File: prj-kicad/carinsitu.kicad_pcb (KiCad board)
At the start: 4 copper layers, 131.5 x 50 mm, 31 parts, among them P1 BAT, P2 MOT, SW1 SWITCH_SLIDE, U1 ESP32, U2 MIC2860, U3 STC3100, X1 40MHz

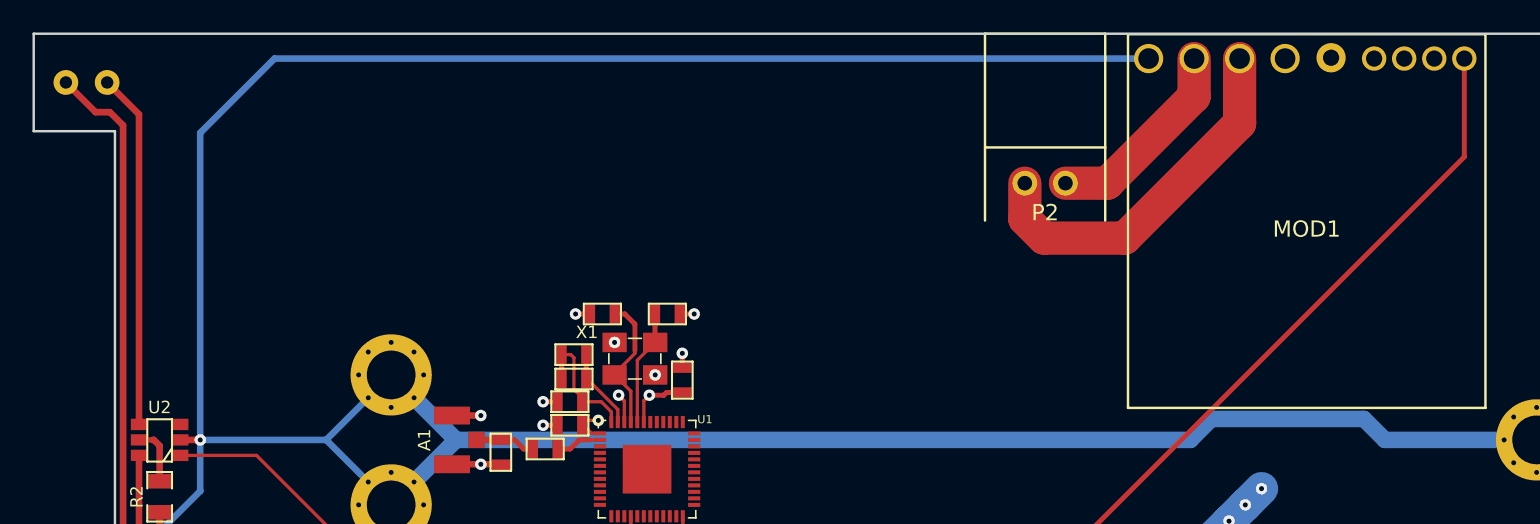
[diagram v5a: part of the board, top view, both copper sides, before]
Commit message: = ADD: insert a 3 pin connector for servo (direction)
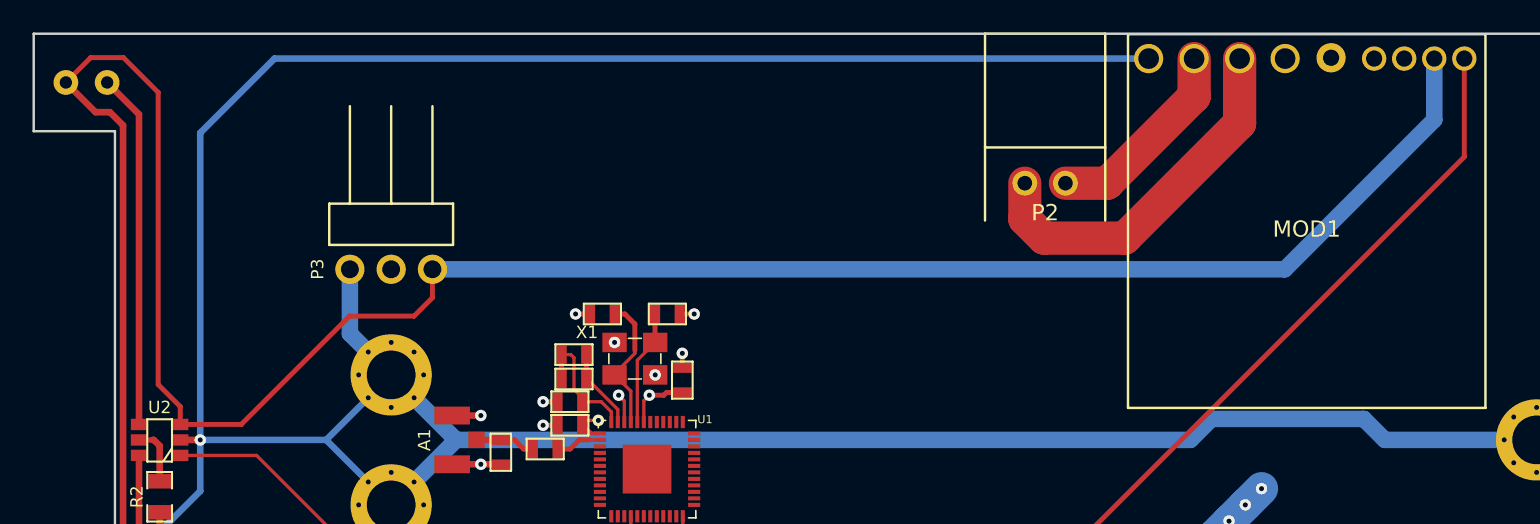
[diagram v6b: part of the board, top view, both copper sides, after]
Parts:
- added P3: CONN_3, carinsitu:CONN_61300311021, F.Cu at (104.8, 94.5)
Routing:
- net +5V: track 48.2 -> 166.1 mm
- net GND: track 309.8 -> 344.2 mm
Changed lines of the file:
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@@
 (kicad_pcb (version 4) (host pcbnew 4.0.2+dfsg1-stable)
   (general
-    (links 99)
-    (no_connects 5)
-    (area 82.674999 79.924999 214.315001 130.075001)
+    (links 101)
+    (no_connects 2)
+    (area 73.750001 78.949999 214.315001 133.950001)
     (thickness 1.6)
     (drawings 27)
-    (tracks 223)
+    (tracks 241)
     (zones 0)
-    (modules 31)
-    (nets 64)
+    (modules 32)
+    (nets 65)
   )
   (page A4)
@@
   )
   (setup
-    (last_trace_width 1.016)
+    (last_trace_width 0.3048)
     (user_trace_width 0.2032)
     (user_trace_width 0.3048)
@@
   (net 62 SDA)
   (net 63 SCL)
+  (net 64 SERVO_PWM)
   (net_class Default "This is the default net class."
     (clearance 0.1524)
@@
     (add_net SCL)
     (add_net SDA)
+    (add_net SERVO_PWM)
   )
   (module carinsitu:FIX locked (layer F.Cu)
@@
     )
   )
+  (module carinsitu:CONN_61300311021 (layer F.Cu)
+    (at 104.75 94.5 180)
+    (fp_text reference P3 (at 4.53 0.01 270) (layer F.SilkS)
+      (effects (font (size 0.762 0.762) (thickness 0.1016)))
+    )
+    (fp_text value CONN_3 (at 0 -1.4 180) (layer F.Fab)
+      (effects (font (size 0.762 0.762) (thickness 0.1016)))
+    )
+    (fp_line (start 2.54 4.04) (end 2.54 10.04) (layer F.SilkS) (width 0.15))
+    (fp_line (start 0 4.04) (end 0 10.04) (layer F.SilkS) (width 0.15))
+    (fp_line (start -2.54 4.04) (end -2.54 10.04) (layer F.SilkS) (width 0.15))
+    (fp_line (start -3.81 1.5) (end 3.81 1.5) (layer F.SilkS) (width 0.15))
+    (fp_line (start 3.81 1.5) (end 3.81 4.04) (layer F.SilkS) (width 0.15))
+    (fp_line (start 3.81 4.04) (end -3.81 4.04) (layer F.SilkS) (width 0.15))
+    (fp_line (start -3.81 4.04) (end -3.81 1.5) (layer F.SilkS) (width 0.15))
+    (pad 1 thru_hole circle (at -2.54 0 180) (size 1.8 1.8) (drill 1.1) (layers *.Cu *.Mask)
+      (net 3 +5V))
+    (pad 2 thru_hole circle (at 0 0 180) (size 1.8 1.8) (drill 1.1) (layers *.Cu *.Mask F.SilkS)
+      (net 64 SERVO_PWM))
+    (pad 3 thru_hole circle (at 2.54 0 180) (size 1.8 1.8) (drill 1.1) (layers *.Cu *.Mask F.SilkS)
+      (net 1 GND))
+  )
   (gr_text + (at 92 121.27) (layer F.SilkS)
     (effects (font (size 1.5 1.5) (thickness 0.3)))
@@
   (gr_line (start 213.21 80) (end 214.24 82.48) (angle 90) (layer Edge.Cuts) (width 0.15))
   (gr_line (start 82.75 80) (end 213.21 80) (angle 90) (layer Edge.Cuts) (width 0.15))
+  (segment (start 167.1 81.53) (end 167.1 96.85) (width 1.016) (layer In2.Cu) (net 1) (status 400000))
+  (segment (start 167.1 96.85) (end 175.25 105) (width 1.016) (layer In2.Cu) (net 1) (status 800000))
+  (segment (start 102.21 94.5) (end 102.21 98.46) (width 1.016) (layer B.Cu) (net 1) (status 400000))
+  (segment (start 102.21 98.46) (end 104.75 101) (width 1.016) (layer B.Cu) (net 1) (status 800000))
   (segment (start 90.5 110.65) (end 90.5 112.03) (width 1.016) (layer B.Cu) (net 1))
   (via (at 92 113.53) (size 0.7112) (drill 0.3048) (layers F.Cu B.Cu) (net 1))
@@
   (segment (start 90.5 112.03) (end 92 113.53) (width 1.016) (layer B.Cu) (net 1))
   (segment (start 93.51 114.8) (end 98.95 114.8) (width 1.016) (layer B.Cu) (net 1))
-  (segment (start 98.95 114.8) (end 104.75 109) (width 1.016) (layer B.Cu) (net 1) (status 800000))
+  (segment (start 98.95 114.8) (end 104.75 109) (width 1.016) (layer B.Cu) (net 1))
   (segment (start 92 114.7975) (end 93.5075 114.7975) (width 1.016) (layer F.Cu) (net 1))
   (segment (start 93.5075 114.7975) (end 93.51 114.8) (width 1.016) (layer F.Cu) (net 1))
@@
   (segment (start 96.685 126.955) (end 96.68 126.95) (width 0.3048) (layer F.Cu) (net 1))
   (via (at 96.68 126.95) (size 0.7112) (drill 0.3048) (layers F.Cu B.Cu) (net 1))
-  (segment (start 97.84 126.955) (end 96.685 126.955) (width 0.3048) (layer F.Cu) (net 1) (status 400000))
+  (segment (start 97.84 126.955) (end 96.685 126.955) (width 0.3048) (layer F.Cu) (net 1))
   (segment (start 94.66 126.95) (end 91 123.29) (width 0.3048) (layer B.Cu) (net 1))
-  (segment (start 100.288 123.33) (end 99.06 123.33) (width 0.3048) (layer F.Cu) (net 1) (status 400000))
+  (segment (start 100.288 123.33) (end 99.06 123.33) (width 0.3048) (layer F.Cu) (net 1))
   (segment (start 98.57 123.29) (end 98.61 123.33) (width 0.3048) (layer B.Cu) (net 1))
   (segment (start 98.61 123.33) (end 99.06 123.33) (width 0.3048) (layer B.Cu) (net 1))
@@
   (via (at 91 123.29) (size 0.7112) (drill 0.3048) (layers F.Cu B.Cu) (net 1))
   (segment (start 91 123.29) (end 98.57 123.29) (width 0.3048) (layer B.Cu) (net 1))
-  (segment (start 100.288 123.33) (end 100.29 123.328) (width 0.3048) (layer F.Cu) (net 1) (status C00000))
+  (segment (start 100.288 123.33) (end 100.29 123.328) (width 0.3048) (layer F.Cu) (net 1))
   (segment (start 122.67 99.67) (end 122.67 100.44) (width 0.3048) (layer In2.Cu) (net 1))
   (segment (start 122.67 100.44) (end 122.11 101) (width 0.3048) (layer In2.Cu) (net 1))
@@
   (segment (start 149.9 92.58) (end 144.93 92.58) (width 2.048) (layer F.Cu) (net 2))
   (segment (start 156.97 85.51) (end 149.9 92.58) (width 2.048) (layer F.Cu) (net 2))
+  (segment (start 91.77 104.0475) (end 91.77 102.95) (width 0.3048) (layer F.Cu) (net 3) (status 400000))
+  (segment (start 86.26 81.47) (end 84.73 83) (width 0.3048) (layer F.Cu) (net 3) (status 800000))
+  (segment (start 88.27 81.47) (end 86.26 81.47) (width 0.3048) (layer F.Cu) (net 3))
+  (segment (start 90.41 83.61) (end 88.27 81.47) (width 0.3048) (layer F.Cu) (net 3))
+  (segment (start 90.41 101.59) (end 90.41 83.61) (width 0.3048) (layer F.Cu) (net 3))
+  (segment (start 91.77 102.95) (end 90.41 101.59) (width 0.3048) (layer F.Cu) (net 3))
+  (segment (start 91.77 104.0475) (end 95.5225 104.0475) (width 0.3048) (layer F.Cu) (net 3) (status 400000))
+  (segment (start 107.29 96.25) (end 107.29 94.5) (width 0.3048) (layer F.Cu) (net 3) (status 800000))
+  (segment (start 106.16 97.38) (end 107.29 96.25) (width 0.3048) (layer F.Cu) (net 3))
+  (segment (start 102.19 97.38) (end 106.16 97.38) (width 0.3048) (layer F.Cu) (net 3))
+  (segment (start 95.5225 104.0475) (end 102.19 97.38) (width 0.3048) (layer F.Cu) (net 3))
+  (segment (start 107.29 94.5) (end 159.75 94.5) (width 1.016) (layer B.Cu) (net 3) (status 400000))
+  (segment (start 168.95 85.3) (end 168.95 81.53) (width 1.016) (layer B.Cu) (net 3) (status 800000))
+  (segment (start 159.75 94.5) (end 168.95 85.3) (width 1.016) (layer B.Cu) (net 3))
   (segment (start 86.56 84.83) (end 87.44 84.83) (width 0.4064) (layer F.Cu) (net 3))
+  (segment (start 87.44 84.83) (end 88.25 85.64) (width 0.4064) (layer F.Cu) (net 3))
+  (segment (start 86.56 84.83) (end 84.73 83) (width 0.4064) (layer F.Cu) (net 3))
+  (segment (start 86.56 125.17) (end 87.81 125.17) (width 0.4064) (layer F.Cu) (net 3))
+  (segment (start 84.73 127) (end 86.56 125.17) (width 0.4064) (layer F.Cu) (net 3))
+  (segment (start 88.25 124.73) (end 88.25 85.64) (width 0.4064) (layer F.Cu) (net 3))
   (segment (start 87.81 125.17) (end 88.25 124.73) (width 0.4064) (layer F.Cu) (net 3))
-  (segment (start 88.25 124.73) (end 88.25 85.64) (width 0.4064) (layer F.Cu) (net 3))
-  (segment (start 84.73 127) (end 86.56 125.17) (width 0.4064) (layer F.Cu) (net 3))
-  (segment (start 86.56 125.17) (end 87.81 125.17) (width 0.4064) (layer F.Cu) (net 3))
-  (segment (start 86.56 84.83) (end 84.73 83) (width 0.4064) (layer F.Cu) (net 3))
-  (segment (start 87.44 84.83) (end 88.25 85.64) (width 0.4064) (layer F.Cu) (net 3))
   (segment (start 89.23 105.9525) (end 89.23 125.04) (width 0.4064) (layer F.Cu) (net 4))
   (segment (start 89.23 125.04) (end 87.27 127) (width 0.4064) (layer F.Cu) (net 4))
@@
   (segment (start 105.48 121.27) (end 107 122.79) (width 2.048) (layer F.Cu) (net 55))
   (segment (start 107 124.25) (end 107 122.79) (width 2.048) (layer F.Cu) (net 55))
-  (segment (start 100.29 124.852) (end 100.29 125.938) (width 0.3048) (layer F.Cu) (net 56) (status C00000))
-  (segment (start 97.84 125.005) (end 99.085 125.005) (width 0.2032) (layer F.Cu) (net 56) (status 400000))
-  (segment (start 99.238 124.852) (end 100.29 124.852) (width 0.2032) (layer F.Cu) (net 56) (status 800000))
+  (segment (start 100.29 124.852) (end 100.29 125.938) (width 0.3048) (layer F.Cu) (net 56))
+  (segment (start 97.84 125.005) (end 99.085 125.005) (width 0.2032) (layer F.Cu) (net 56))
+  (segment (start 99.238 124.852) (end 100.29 124.852) (width 0.2032) (layer F.Cu) (net 56))
   (segment (start 99.085 125.005) (end 99.238 124.852) (width 0.2032) (layer F.Cu) (net 56))
   (segment (start 105 125.11) (end 103.52 125.11) (width 0.3048) (layer F.Cu) (net 57))

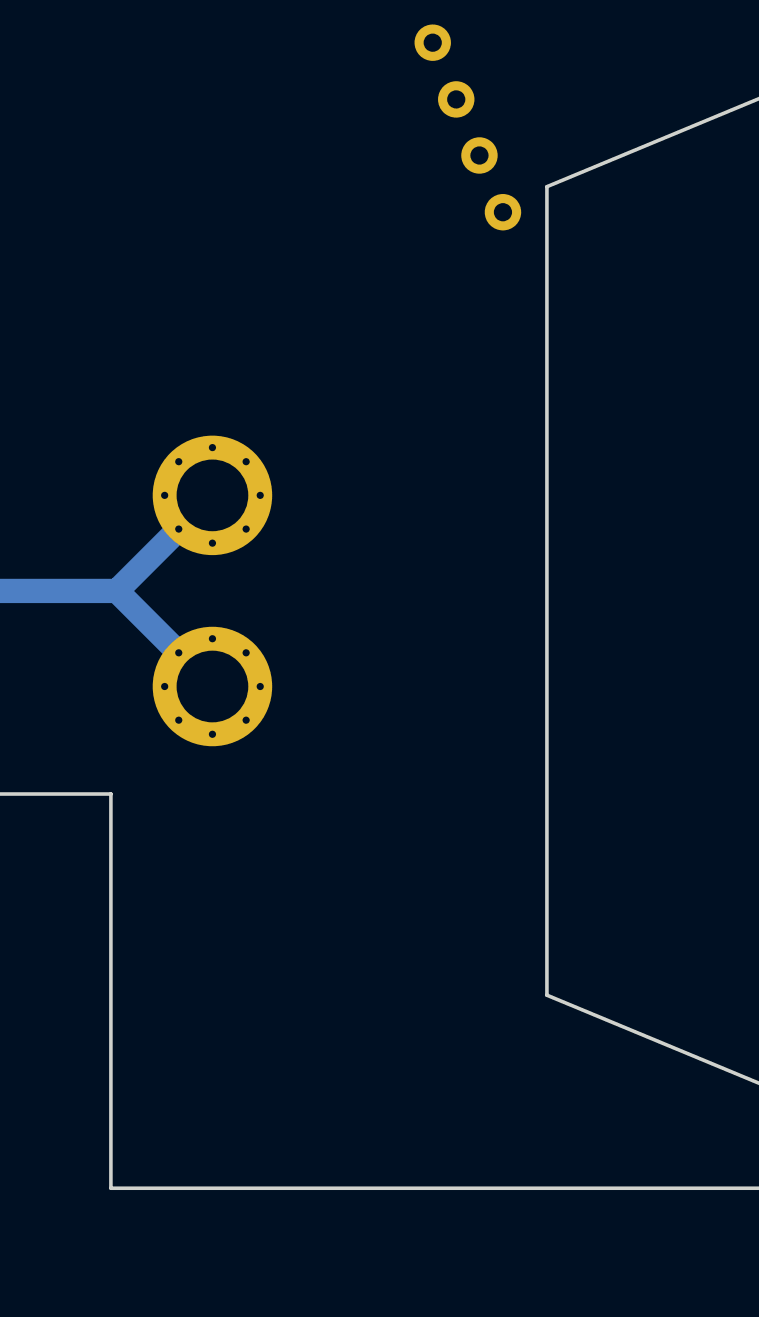
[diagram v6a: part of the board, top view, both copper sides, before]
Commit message: = ADD: insert second RGB led and add a level switch (3V3 -> 5V) on data line
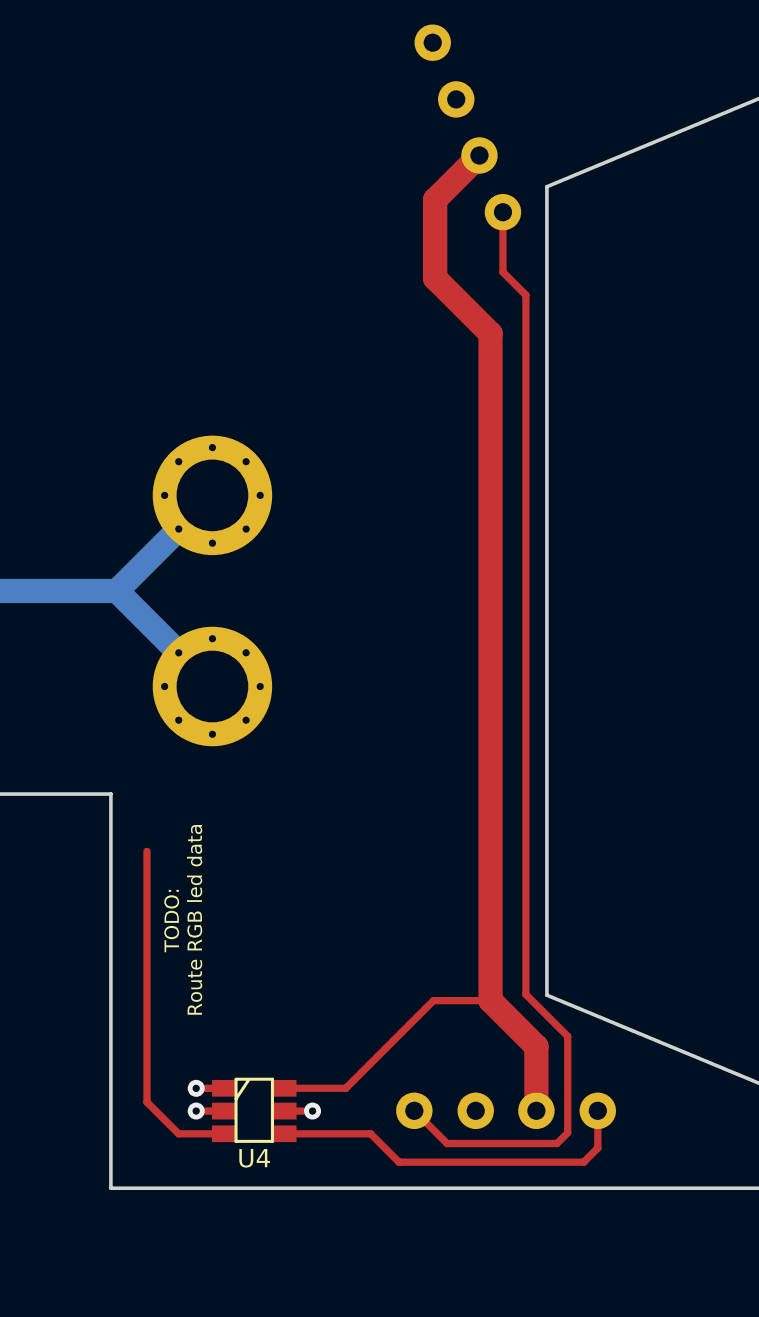
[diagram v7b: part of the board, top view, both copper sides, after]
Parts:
- added D3: LED_APA106, carinsitu:LED-APA106, F.Cu at (199.0, 126.8)
- added U4: SN74LVC1T45, carinsitu:SOT23-6, F.Cu at (188.5, 126.8)
- D4: renamed from REF**; value LED-APA106 -> LED_APA106
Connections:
- D4 pad 1: (no net) -> Net-(D4-Pad1)
- D4 pad 2: (no net) -> GND
- D4 pad 3: (no net) -> +5V
- D4 pad 4: (no net) -> Net-(D3-Pad1)
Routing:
- net GND: track 344.2 -> 404.5 mm, vias 17 -> 18
- net +5V: track 166.1 -> 218.8 mm
- net Net-(D3-Pad1): track 0.00 -> 46.8 mm
- net +3V3: track 12.1 -> 53.7 mm, vias 3 -> 5
- net Net-(D3-Pad4): track 0.00 -> 15.4 mm
- net RL_DAT: track 0.00 -> 14.3 mm
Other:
- board text added: "TODO: Route RGB led data"

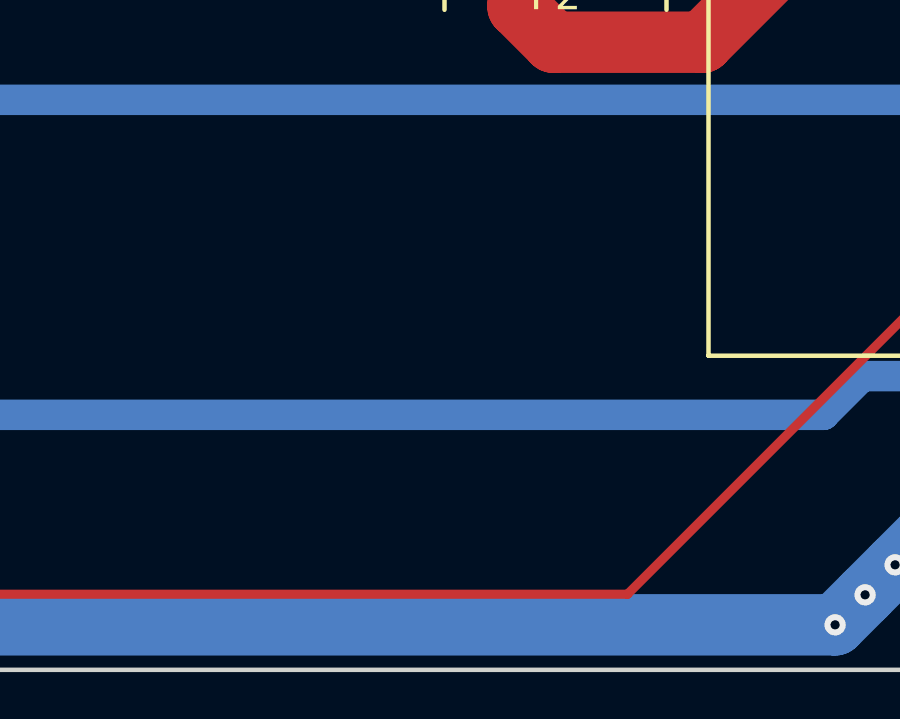
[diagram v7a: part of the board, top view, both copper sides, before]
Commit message: = ADD: insert a 3V3 power regulator. Schematic and place ok, routing not complete
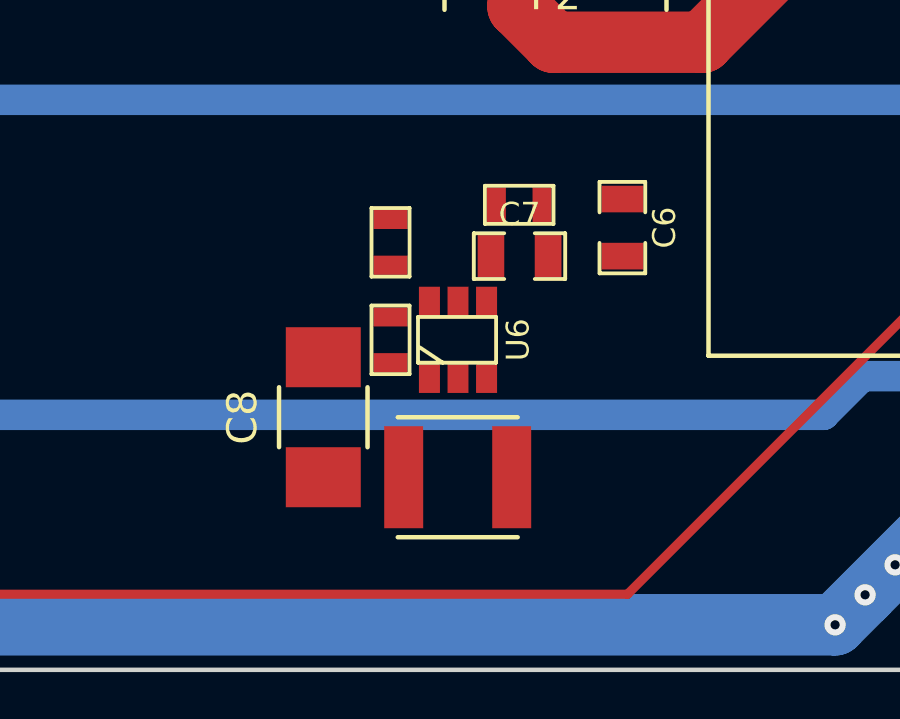
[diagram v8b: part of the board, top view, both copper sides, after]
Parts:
- added C6: C, carinsitu:SMD0805, F.Cu at (147.2, 98.8)
- added C7: C, carinsitu:SMD0805, F.Cu at (143.8, 99.7)
- added C8: C, carinsitu:SMD1210, F.Cu at (137.3, 105.1)
- added L2: FB600, carinsitu:SMD0603, F.Cu at (143.8, 98.0)
- added L3: 4,7uH, carinsitu:I_TYS4012, F.Cu at (141.7, 107.1)
- added R6: 150k, carinsitu:SMD0603, F.Cu at (139.5, 102.5)
- added R7: 48,7k, carinsitu:SMD0603, F.Cu at (139.5, 99.2)
- added U6: TPS560200, carinsitu:SOT23-6, F.Cu at (141.8, 102.5)
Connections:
- MOD1 pad 2: GND -> Net-(MOD1-Pad2)
- MOD1 pad 6: Net-(MOD1-Pad6) -> Net-(MOD1-Pad5)
- P2 pad 1: GND -> Net-(MOD1-Pad2)
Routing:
- net GND: track 404.5 -> 392.1 mm
- net Net-(MOD1-Pad2): track 0.00 -> 12.5 mm
